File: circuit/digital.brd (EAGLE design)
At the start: 56.2 x 50.8 mm, 35 parts, among them IC1 MCP1701-5V, IC2 MCP1700-3.3V, X1 MINI-USB-SCHIELD-32005-301

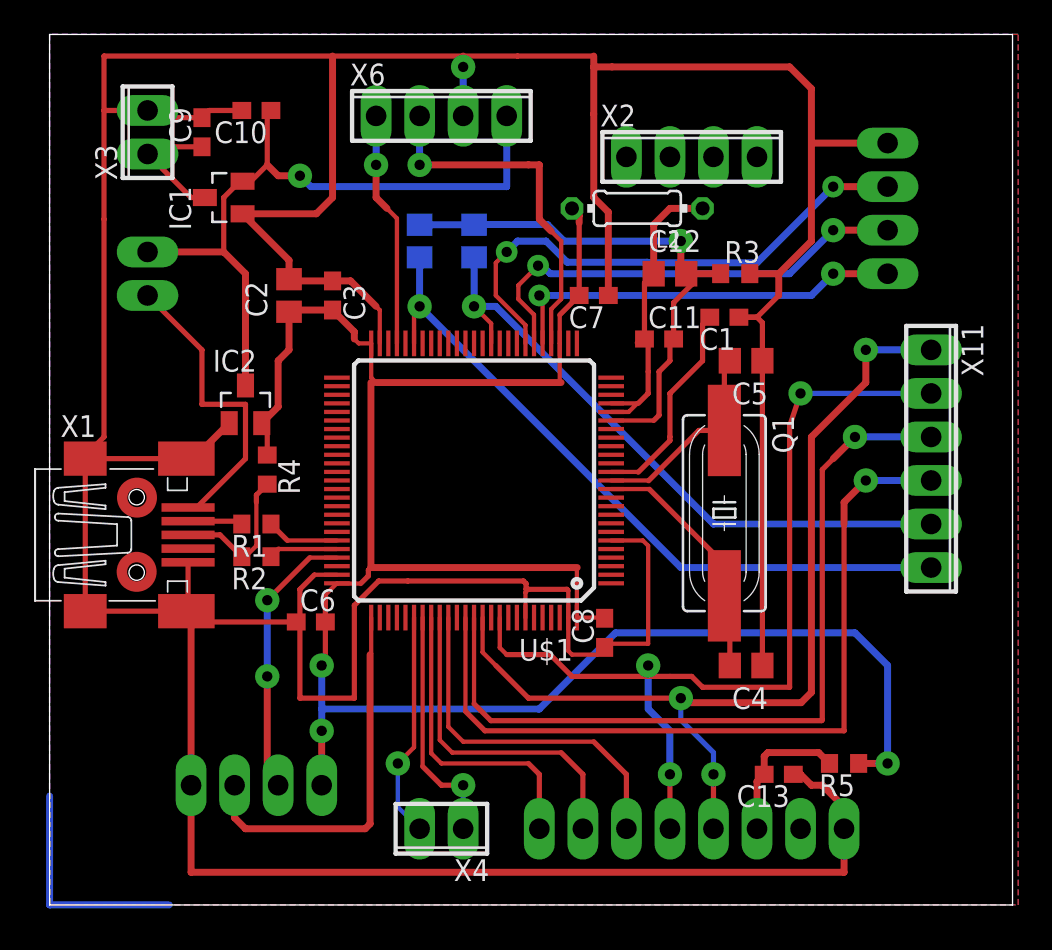
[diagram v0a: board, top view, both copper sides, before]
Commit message: - переместили схемы чуть ниже, чтобы уместиться в 49 мм высоты
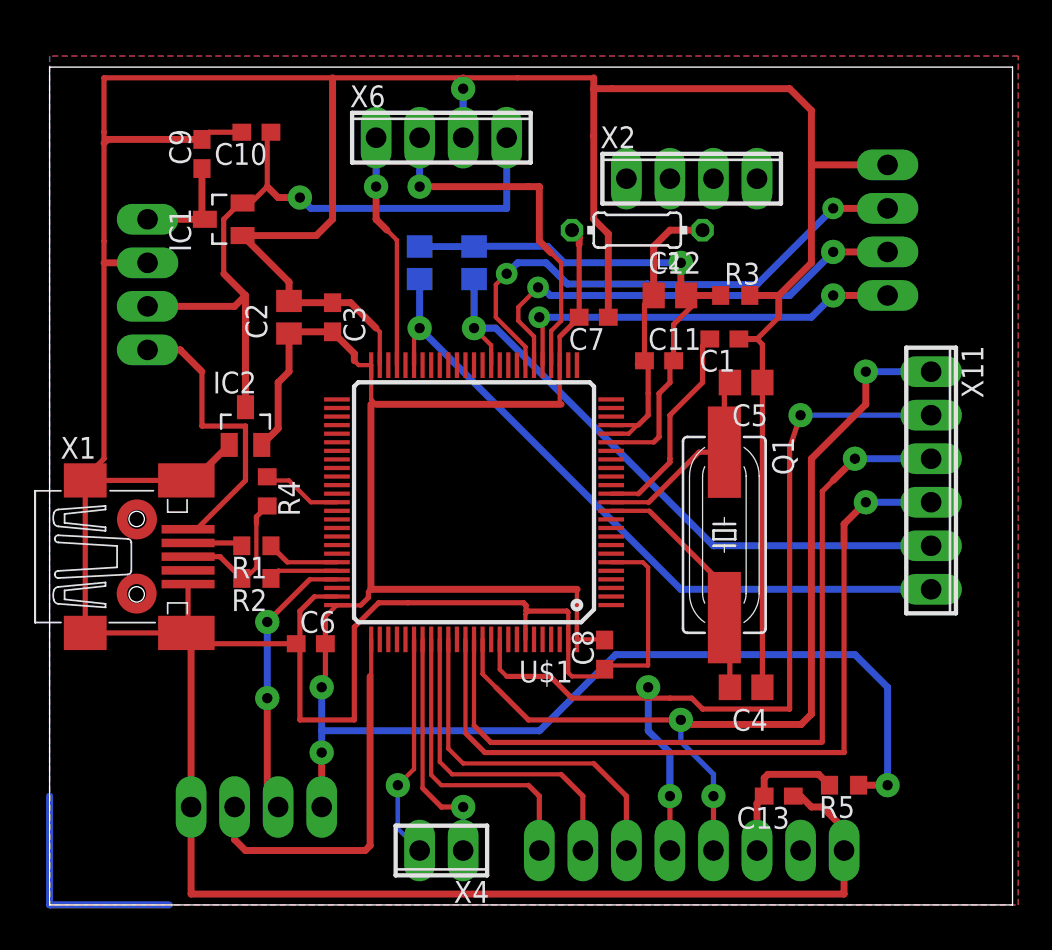
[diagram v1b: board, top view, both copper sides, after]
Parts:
- removed X3, X5: (no value), con-phoenix-254:2POL254
- added X8: (no value), con-phoenix-254:4POL254
- moved C11 1.27 mm to (35.6, 31.8)
- moved C2 1.27 mm to (14.0, 34.3)
- moved C3 1.27 mm to (16.5, 34.3)
- moved C7 1.27 mm to (31.8, 34.3)
- moved C9 1.27 mm to (8.89, 43.8)
- moved L2 1.27 mm to (34.3, 39.4)
- moved R1 1.27 mm to (12.1, 21.0)
- moved X2 1.27 mm to (37.5, 42.4)
- moved X6 1.27 mm to (22.9, 44.8)
- moved X7 1.27 mm to (48.9, 39.4)
- moved C4 1.27 mm to (40.6, 12.7)
- moved C6 1.27 mm to (15.2, 15.2)
- moved C13 1.27 mm to (42.5, 6.35)
- moved DISPLAY 1.27 mm to (37.5, 3.17)
- moved R5 1.27 mm to (46.4, 6.99)
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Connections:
- new net USB_ON: R4.1, U$1.63
- net +3V3: no longer R4.1
- net +5V: now also X8.3; no longer X5.2
- net GND: now also X8.2; no longer X3.2
- net N$7: now also X8.1; no longer X3.1
- net N$8: now also X8.4; no longer X5.1
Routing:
- net USB_ON: track 0.00 -> 4.68 mm
- net GND: track 305.6 -> 308.1 mm
- net +3V3: track 124.6 -> 123.0 mm
- net +5V: track 41.4 -> 42.9 mm
- net N$7: track 7.75 -> 6.38 mm
- net N$8: track 17.9 -> 17.1 mm
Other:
- board size 56.2 x 50.8 mm -> 56.2 x 48.9 mm

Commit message: - по краям насечки для винтов
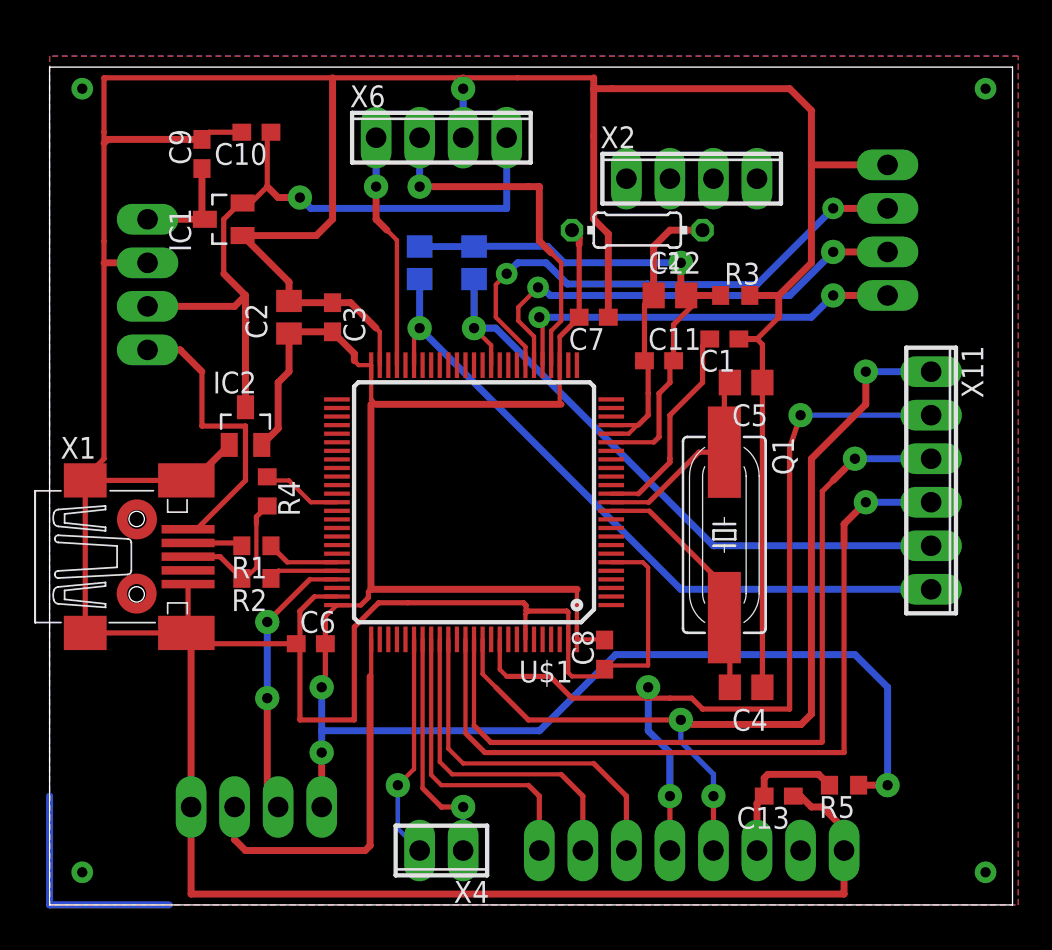
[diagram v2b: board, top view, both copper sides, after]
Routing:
- net GND: vias 1 -> 5
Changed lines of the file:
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@@
 <wire x1="3.39" y1="44.665" x2="3.175" y2="44.45" width="0.4064" layer="1"/>
 <wire x1="5.715" y1="37.465" x2="3.175" y2="37.465" width="0.4064" layer="1"/>
+<via x="1.905" y="47.625" extent="1-16" drill="0.6" diameter="1.27"/>
+<via x="54.61" y="47.625" extent="1-16" drill="0.6" diameter="1.27"/>
+<via x="54.61" y="1.905" extent="1-16" drill="0.6" diameter="1.27"/>
+<via x="1.905" y="1.905" extent="1-16" drill="0.6" diameter="1.27"/>
+<wire x1="8.255" y1="0.635" x2="1.905" y2="1.905" width="0" layer="19" extent="1-1"/>
 </signal>
 <signal name="N$3">

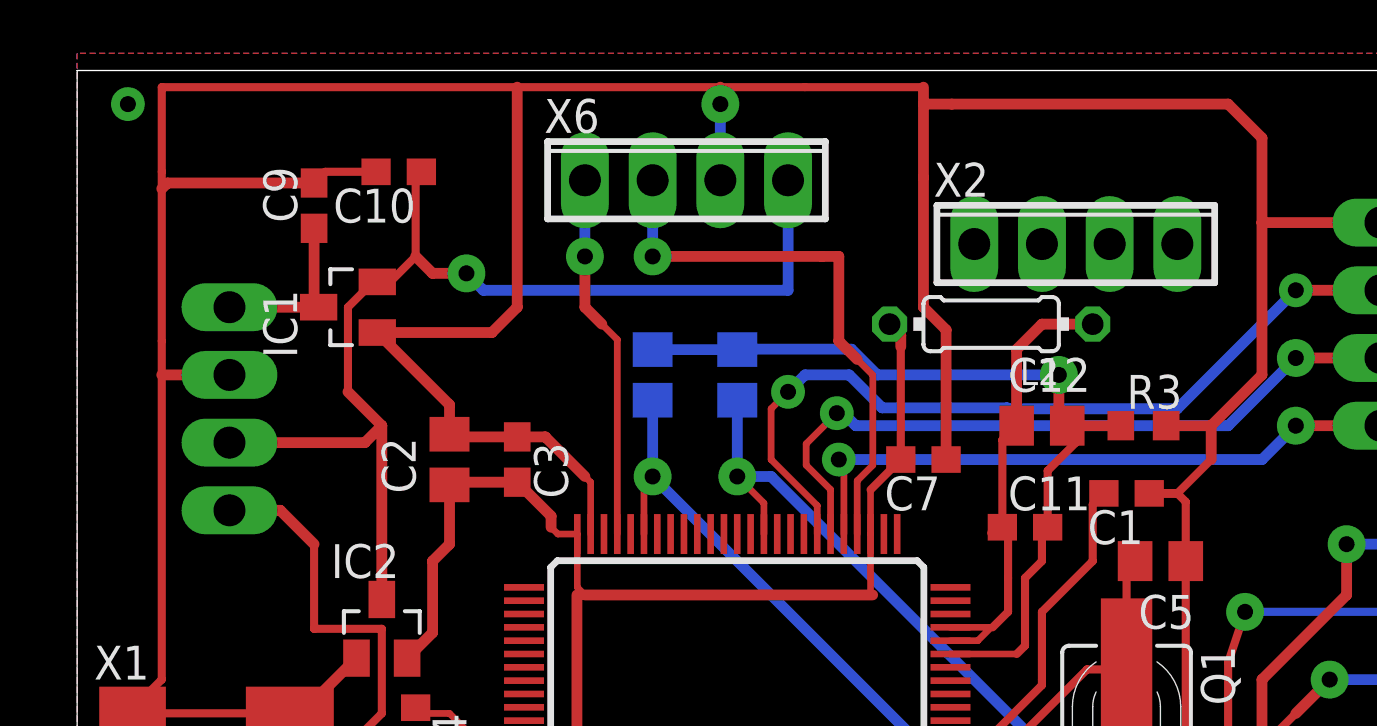
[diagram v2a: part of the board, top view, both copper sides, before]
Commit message: - слили вместе GND и GNDA - добавили измерение VBAT напряжения
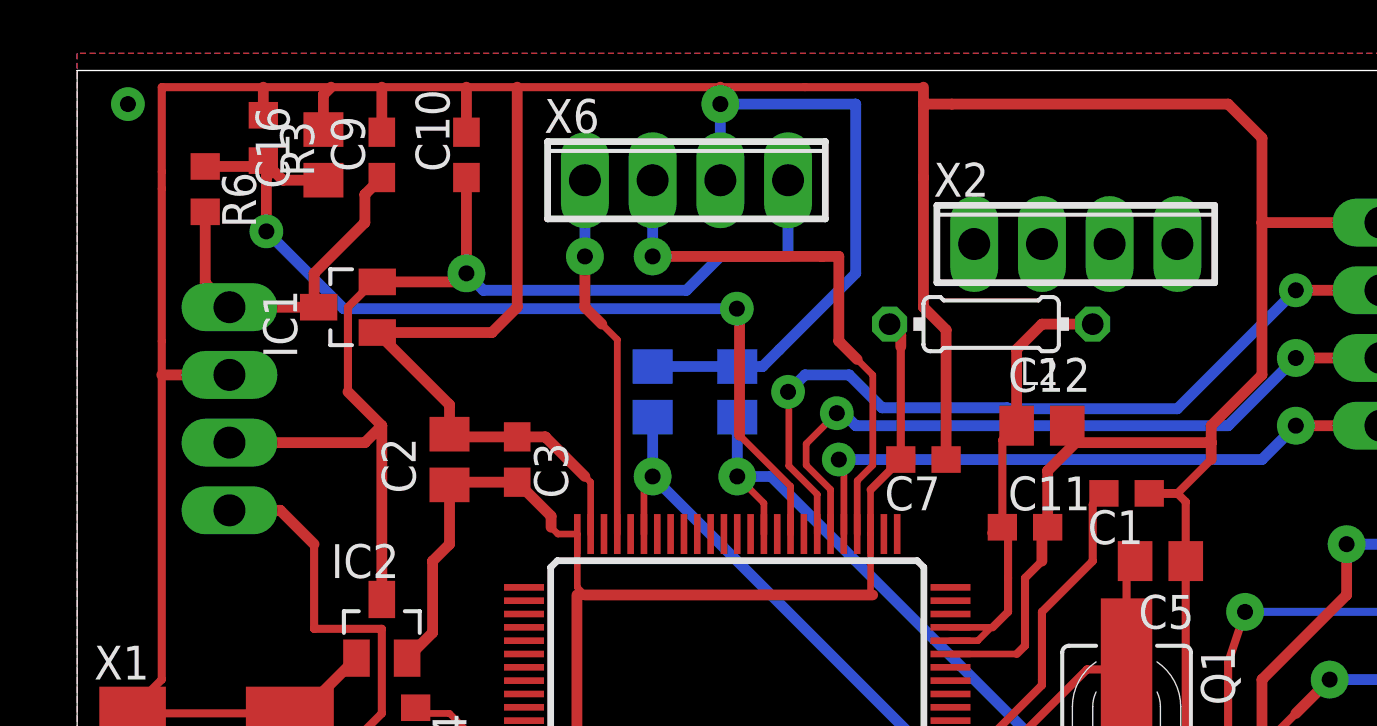
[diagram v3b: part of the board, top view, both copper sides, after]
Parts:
- added C16: 2.2n, rcl:C0805
- added R6: 3.3K, rcl:R0603
- R3: value 0 -> 2.2K
- moved R3 34.7 mm to (6.99, 46.4), turned to 270 degrees
- moved C9 3.18 mm to (11.4, 45.7)
- moved C10 2.62 mm to (14.6, 45.7), turned to 90 degrees
- moved C14 0.64 mm to (21.6, 36.8)
- moved C15 0.64 mm to (24.8, 36.8)
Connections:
- removed net GNDA: C11.2, C12.2, C14.2, C15.2, R3.1, U$1.20
- new net ADC_BAT: C16.1, R3.2, R6.1, U$1.34
- net GND: now also C11.2, C12.2, C14.2, C15.2, C16.2, R3.1, U$1.20; no longer R3.2
- net N$7: now also R6.2
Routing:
- net ADC_BAT: track 0.00 -> 35.4 mm, vias 0 -> 2
- net GND: track 308.1 -> 341.9 mm
- net GNDA: track 31.8 -> 0.00 mm, vias 1 -> 0
- net N$7: track 6.38 -> 13.3 mm
- net +5V: track 42.9 -> 41.7 mm
- net V_ADC: track 37.4 -> 36.7 mm
- net I_ADC: track 41.3 -> 40.7 mm
- net ENC_B: track 31.2 -> 30.6 mm

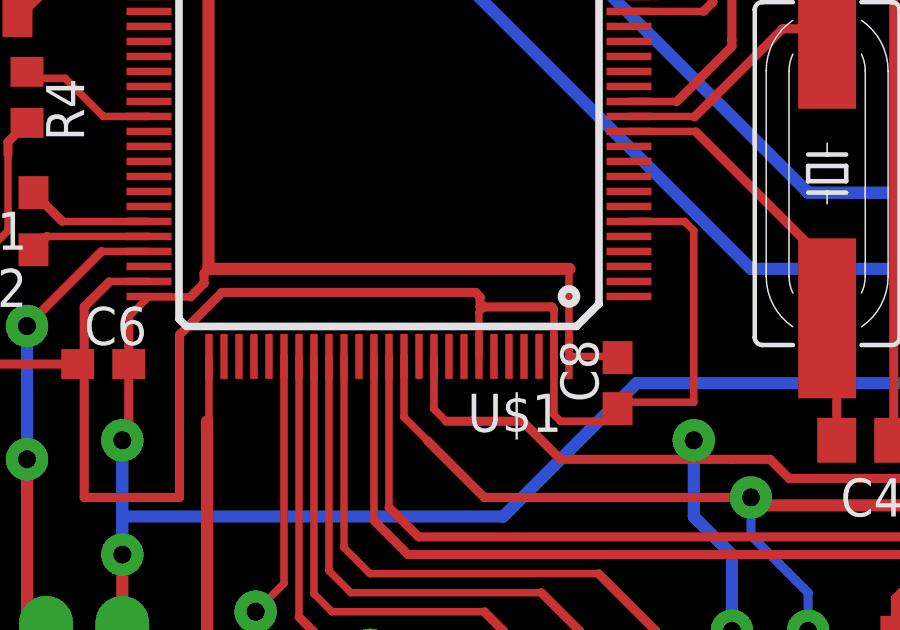
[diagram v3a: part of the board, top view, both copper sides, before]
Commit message: - Vbat таки подключать к питанию, а не к земле
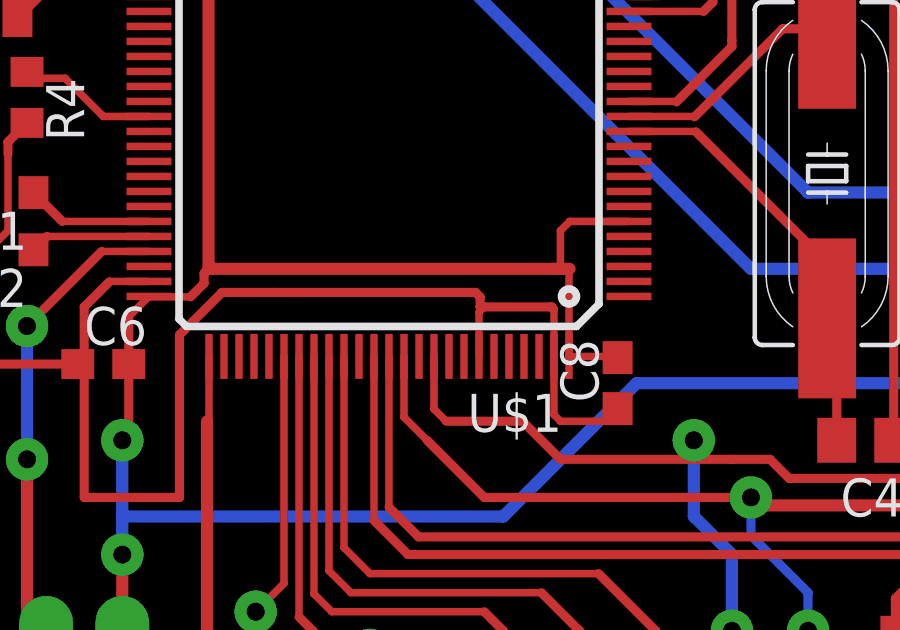
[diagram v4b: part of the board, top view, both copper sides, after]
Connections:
- net +3V3: now also U$1.6
- net GND: no longer U$1.6
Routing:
- net GND: track 341.9 -> 331.3 mm
- net +3V3: track 123.0 -> 126.7 mm
- added copper zone on layer 16, net GND
- removed copper zone on layer 16, net GNDA

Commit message: - завели софтварный SPI1
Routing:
- net N$12: track 0.00 -> 14.6 mm
- net N$11: track 0.00 -> 14.6 mm
- net N$10: track 0.00 -> 13.3 mm
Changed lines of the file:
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@@
 <layers>
 <layer number="1" name="Top" color="4" fill="1" visible="yes" active="yes"/>
-<layer number="16" name="Bottom" color="1" fill="1" visible="yes" active="yes"/>
+<layer number="16" name="Bottom" color="1" fill="1" visible="no" active="yes"/>
 <layer number="17" name="Pads" color="2" fill="1" visible="yes" active="yes"/>
 <layer number="18" name="Vias" color="2" fill="1" visible="yes" active="yes"/>
-<layer number="19" name="Unrouted" color="6" fill="1" visible="yes" active="yes"/>
+<layer number="19" name="Unrouted" color="6" fill="1" visible="no" active="yes"/>
 <layer number="20" name="Dimension" color="15" fill="1" visible="no" active="yes"/>
 <layer number="21" name="tPlace" color="7" fill="1" visible="no" active="yes"/>
@@
 <vertex x="0" y="49.53"/>
 </polygon>
-<wire x1="48.895" y1="43.18" x2="54.61" y2="47.625" width="0" layer="19" extent="1-1"/>
-<wire x1="2.08" y1="24.77" x2="1.905" y2="24.765" width="0" layer="19" extent="1-1"/>
-<wire x1="1.905" y1="47.625" x2="3.175" y2="48.26" width="0" layer="19" extent="1-1"/>
-<wire x1="1.905" y1="1.905" x2="8.255" y2="0.635" width="0" layer="19" extent="1-1"/>
-<wire x1="54.61" y1="1.905" x2="46.355" y2="3.175" width="0" layer="19" extent="1-1"/>
 </signal>
 <signal name="N$3">
@@
 <wire x1="7.1" y1="44.9" x2="7.345" y2="45.145" width="0.4064" layer="1"/>
 </signal>
+<signal name="N$10">
+<wire x1="6.985" y1="0" x2="0" y2="0" width="0.4064" layer="1"/>
+<wire x1="0" y1="0" x2="0" y2="6.35" width="0.4064" layer="1"/>
+</signal>
+<signal name="N$11">
+<wire x1="48.26" y1="0" x2="55.88" y2="0" width="0.4064" layer="1"/>
+<wire x1="55.88" y1="0" x2="55.88" y2="6.985" width="0.4064" layer="1"/>
+</signal>
+<signal name="N$12">
+<wire x1="48.26" y1="0" x2="55.88" y2="0" width="0.4064" layer="16"/>
+<wire x1="55.88" y1="0" x2="55.88" y2="6.985" width="0.4064" layer="16"/>
+</signal>
 </signals>
